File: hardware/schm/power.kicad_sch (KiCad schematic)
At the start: 14 parts, among them J1 VBUS input fly-leads, U2 AP63205WU-7

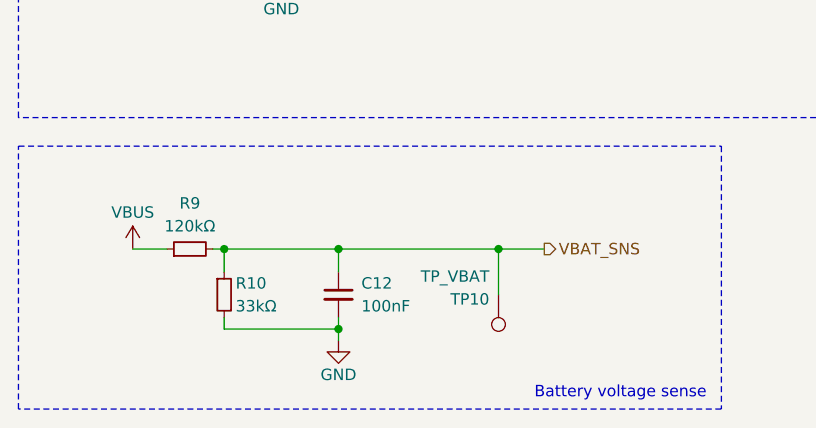
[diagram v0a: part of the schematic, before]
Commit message: feat: swap to the 74HC595 for cs expansion
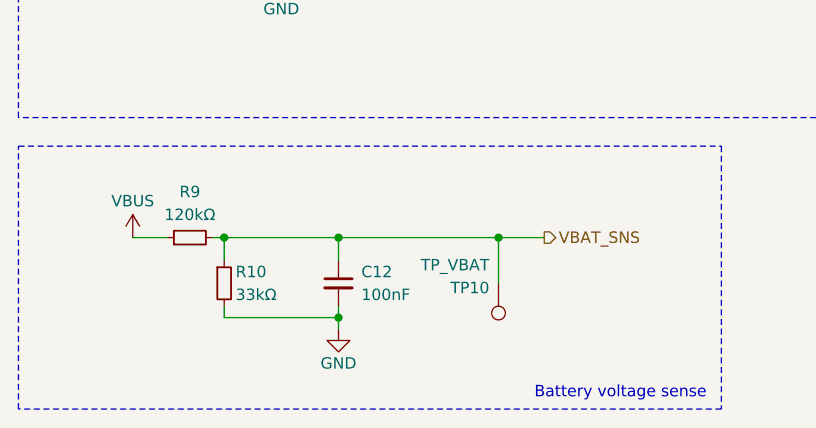
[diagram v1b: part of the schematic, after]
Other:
- moved on the sheet: C12, R10, R9, TP10
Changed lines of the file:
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@@
 	)
 	(junction
-		(at 68.58 74.93)
+		(at 68.58 73.66)
 		(diameter 0)
 		(color 0 0 0 0)
@@
 	)
 	(junction
-		(at 50.8 83.82)
+		(at 50.8 82.55)
 		(diameter 0)
 		(color 0 0 0 0)
 	)
 	(junction
-		(at 50.8 74.93)
+		(at 50.8 73.66)
 		(diameter 0)
 		(color 0 0 0 0)
 	)
 	(junction
-		(at 38.1 74.93)
+		(at 38.1 73.66)
 		(diameter 0)
 		(color 0 0 0 0)
@@
 	(wire
 		(pts
-			(xy 50.8 83.82) (xy 38.1 83.82)
+			(xy 50.8 82.55) (xy 38.1 82.55)
 		)
 		(stroke
@@
 	(wire
 		(pts
-			(xy 68.58 74.93) (xy 73.66 74.93)
+			(xy 68.58 73.66) (xy 73.66 73.66)
 		)
 		(stroke
@@
 	(wire
 		(pts
-			(xy 38.1 74.93) (xy 38.1 77.47)
+			(xy 38.1 73.66) (xy 38.1 76.2)
 		)
 		(stroke
@@
 	(wire
 		(pts
-			(xy 38.1 74.93) (xy 50.8 74.93)
+			(xy 38.1 73.66) (xy 50.8 73.66)
 		)
 		(stroke
@@
 	(wire
 		(pts
-			(xy 36.83 74.93) (xy 38.1 74.93)
+			(xy 36.83 73.66) (xy 38.1 73.66)
 		)
 		(stroke
@@
 	(wire
 		(pts
-			(xy 50.8 83.82) (xy 50.8 85.09)
-		)
-		(stroke
-			(width 0)
-			(type default)
-		)
-	)
-	(wire
-		(pts
-			(xy 68.58 74.93) (xy 68.58 80.01)
-		)
-		(stroke
-			(width 0)
-			(type default)
-		)
-	)
-	(wire
-		(pts
-			(xy 50.8 74.93) (xy 50.8 77.47)
+			(xy 50.8 82.55) (xy 50.8 83.82)
+		)
+		(stroke
+			(width 0)
+			(type default)
+		)
+	)
+	(wire
+		(pts
+			(xy 68.58 73.66) (xy 68.58 78.74)
+		)
+		(stroke
+			(width 0)
+			(type default)
+		)
+	)
+	(wire
+		(pts
+			(xy 50.8 73.66) (xy 50.8 76.2)
 		)
 		(stroke
@@
 	(wire
 		(pts
-			(xy 38.1 83.82) (xy 38.1 82.55)
+			(xy 38.1 82.55) (xy 38.1 81.28)
 		)
 		(stroke
@@
 	(wire
 		(pts
-			(xy 50.8 74.93) (xy 68.58 74.93)
+			(xy 50.8 73.66) (xy 68.58 73.66)
 		)
 		(stroke
@@
 	(wire
 		(pts
-			(xy 27.94 74.93) (xy 31.75 74.93)
+			(xy 27.94 73.66) (xy 31.75 73.66)
 		)
 		(stroke
@@
 	(wire
 		(pts
-			(xy 50.8 82.55) (xy 50.8 83.82)
+			(xy 50.8 81.28) (xy 50.8 82.55)
 		)
 		(stroke
@@
 	(hierarchical_label "VBAT_SNS"
 		(shape output)
-		(at 73.66 74.93 0)
+		(at 73.66 73.66 0)
 		(effects
 			(font
@@
 	(symbol
 		(lib_id "Device:R_Small")
-		(at 38.1 80.01 0)
+		(at 38.1 78.74 0)
 		(unit 1)
 		(body_style 1)
@@
 		(fields_autoplaced yes)
 		(property "Reference" "R10"
-			(at 39.37 78.74 0)
+			(at 39.37 77.47 0)
 			(show_name no)
 			(do_not_autoplace no)
@@
 		)
 		(property "Value" "33kΩ"
-			(at 39.37 81.28 0)
+			(at 39.37 80.01 0)
 			(show_name no)
 			(do_not_autoplace no)
@@
 		)
 		(property "Footprint" "Resistor_SMD:R_0402_1005Metric"
-			(at 38.1 80.01 0)
+			(at 38.1 78.74 0)
 			(hide yes)
 			(show_name no)
@@
 		)
 		(property "Datasheet" "~"
-			(at 38.1 80.01 0)
+			(at 38.1 78.74 0)
 			(hide yes)
 			(show_name no)
@@
 		)
 		(property "Description" ""
-			(at 38.1 80.01 0)
+			(at 38.1 78.74 0)
 			(show_name no)
 			(do_not_autoplace no)
@@
 		)
 		(property "LCSC Part" "NONE"
-			(at -312.42 -48.26 0)
+			(at -312.42 -49.53 0)
 			(hide yes)
 			(show_name no)
@@
 	(symbol
 		(lib_id "Device:R_Small")
-		(at 34.29 74.93 90)
+		(at 34.29 73.66 90)
 		(unit 1)
 		(body_style 1)
@@
 		(fields_autoplaced yes)
 		(property "Reference" "R9"
-			(at 34.29 69.85 90)
+			(at 34.29 68.58 90)
 			(show_name no)
 			(do_not_autoplace no)
@@
 		)
 		(property "Value" "120kΩ"
-			(at 34.29 72.39 90)
+			(at 34.29 71.12 90)
 			(show_name no)
 			(do_not_autoplace no)
@@
 		)
 		(property "Footprint" "Resistor_SMD:R_0402_1005Metric"
-			(at 34.29 74.93 0)
+			(at 34.29 73.66 0)
 			(hide yes)
 			(show_name no)
@@
 		)
 		(property "Datasheet" "~"
-			(at 34.29 74.93 0)
+			(at 34.29 73.66 0)
 			(hide yes)
 			(show_name no)
@@
 		)
 		(property "Description" ""
-			(at 34.29 74.93 0)
+			(at 34.29 73.66 0)
 			(show_name no)
 			(do_not_autoplace no)
@@
 		)
 		(property "LCSC Part" "NONE"
-			(at -83.82 425.45 0)
+			(at -83.82 424.18 0)
 			(hide yes)
 			(show_name no)
@@
 	(symbol
 		(lib_id "power:VBUS")
-		(at 27.94 74.93 0)
+		(at 27.94 73.66 0)
 		(unit 1)
 		(body_style 1)
@@
 		(dnp no)
 		(property "Reference" "#PWR075"
-			(at 27.94 71.12 0)
+			(at 27.94 69.85 0)
 			(hide yes)
 			(show_name no)
@@
 		)
 		(property "Value" "VBUS"
-			(at 27.94 70.866 0)
+			(at 27.94 69.596 0)
 			(show_name no)
 			(do_not_autoplace no)
@@
 		)
 		(property "Footprint" ""
-			(at 27.94 74.93 0)
+			(at 27.94 73.66 0)
 			(show_name no)
 			(do_not_autoplace no)
@@
 		)
 		(property "Datasheet" "~"
-			(at 27.94 74.93 0)
+			(at 27.94 73.66 0)
 			(hide yes)
 			(show_name no)
@@
 		)
 		(property "Description" ""
-			(at 27.94 74.93 0)
+			(at 27.94 73.66 0)
 			(show_name no)
 			(do_not_autoplace no)
@@
 	(symbol
 		(lib_id "power:GND")
-		(at 50.8 85.09 0)
+		(at 50.8 83.82 0)
 		(unit 1)
 		(body_style 1)
@@
 		(fields_autoplaced yes)
 		(property "Reference" "#PWR073"
+			(at 50.8 86.36 0)
+			(hide yes)
+			(show_name no)
+			(do_not_autoplace no)
+			(effects
+				(font
+					(size 1.27 1.27)
+				)
+			)
+		)
+		(property "Value" "GND"
 			(at 50.8 87.63 0)
-			(hide yes)
-			(show_name no)
-			(do_not_autoplace no)
-			(effects
-				(font
-					(size 1.27 1.27)
-				)
-			)
-		)
-		(property "Value" "GND"
-			(at 50.8 88.9 0)
 			(show_name no)
 			(do_not_autoplace no)
@@
 		)
 		(property "Footprint" ""
-			(at 50.8 85.09 0)
+			(at 50.8 83.82 0)
 			(show_name no)
 			(do_not_autoplace no)
@@
 		)
 		(property "Datasheet" "~"
-			(at 50.8 85.09 0)
+			(at 50.8 83.82 0)
 			(hide yes)
 			(show_name no)
@@
 		)
 		(property "Description" ""
-			(at 50.8 85.09 0)
+			(at 50.8 83.82 0)
 			(show_name no)
 			(do_not_autoplace no)
@@
 	(symbol
 		(lib_id "Connector:TestPoint")
-		(at 68.58 80.01 180)
+		(at 68.58 78.74 180)
 		(unit 1)
 		(body_style 1)
@@
 		(dnp no)
 		(property "Reference" "TP10"
-			(at 67.564 80.518 0)
+			(at 67.564 79.248 0)
 			(show_name no)
 			(do_not_autoplace no)
@@
 		)
 		(property "Value" "TP_VBAT"
-			(at 67.564 77.978 0)
+			(at 67.564 76.708 0)
 			(show_name no)
 			(do_not_autoplace no)
@@
 		)
 		(property "Footprint" "TestPoint:TestPoint_Pad_D1.0mm"
-			(at 68.58 80.01 0)
+			(at 68.58 78.74 0)
 			(hide yes)
 			(show_name no)
@@
 		)
 		(property "Datasheet" "~"
-			(at 68.58 80.01 0)
+			(at 68.58 78.74 0)
 			(hide yes)
 			(show_name no)
@@
 		)
 		(property "Description" ""
-			(at 68.58 80.01 0)
+			(at 68.58 78.74 0)
 			(show_name no)
 			(do_not_autoplace no)
@@
 		)
 		(property "LCSC Part" "NONE"
-			(at 412.75 203.2 0)
+			(at 412.75 201.93 0)
 			(hide yes)
 			(show_name no)
@@
 	(symbol
 		(lib_id "Device:C_Small")
-		(at 50.8 80.01 0)
+		(at 50.8 78.74 0)
 		(unit 1)
 		(body_style 1)
@@
 		(fields_autoplaced yes)
 		(property "Reference" "C12"
-			(at 53.34 78.74 0)
+			(at 53.34 77.47 0)
 			(show_name no)
 			(do_not_autoplace no)
@@
 		)
 		(property "Value" "100nF"
-			(at 53.34 81.28 0)
+			(at 53.34 80.01 0)
 			(show_name no)
 			(do_not_autoplace no)
@@
 		)
 		(property "Footprint" "Capacitor_SMD:C_0402_1005Metric"
-			(at 50.8 80.01 0)
+			(at 50.8 78.74 0)
 			(hide yes)
 			(show_name no)
@@
 		)
 		(property "Datasheet" "~"
-			(at 50.8 80.01 0)
+			(at 50.8 78.74 0)
 			(hide yes)
 			(show_name no)
@@
 		)
 		(property "Description" ""
-			(at 50.8 80.01 0)
+			(at 50.8 78.74 0)
 			(show_name no)
 			(do_not_autoplace no)
@@
 		)
 		(property "LCSC Part" "NONE"
-			(at -307.34 -45.72 0)
-			(hide yes)
-			(show_name no)
+			(at -307.34 -46.99 0)
+			(hide yes)
+			(show_name no)

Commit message: feat: first bit of routing and double leds + fixes
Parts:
- added C13: 10uF, Capacitor_SMD:C_0603_1608Metric, symbol Device:C_Small
- J1: footprint Connector_Wire:SolderWire-0.5sqmm_1x02_P4.6mm_D0.9mm_OD2.1mm_Relief -> Connector_Wire:SolderWire-0.25sqmm_1x02_P4.2mm_D0.65mm_OD1.7mm
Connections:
- net 3V3: now also C13.1
- net GND: now also C13.2
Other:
- moved on the sheet: C6

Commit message: feat: add bom placement
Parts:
- C1, C4, C5: LCSC Part NONE -> C602037
- C12, C2, C3: LCSC Part NONE -> C169834
- C13, C6: LCSC Part NONE -> C913532
- J1, TP10: now left out of the parts list
- R10: value 33kΩ -> 33.2kΩ; LCSC Part NONE -> C3008937
- R9: LCSC Part NONE -> C409883
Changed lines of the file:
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@@
 			)
 		)
-		(property "LCSC Part" "NONE"
+		(property "LCSC Part" "C169834"
 			(at 152.4 -59.69 0)
 			(hide yes)
@@
 			)
 		)
-		(property "LCSC Part" "NONE"
+		(property "LCSC Part" "C169834"
 			(at 17.78 1.27 0)
 			(hide yes)
@@
 			)
 		)
-		(property "Value" "33kΩ"
+		(property "Value" "33.2kΩ"
 			(at 39.37 80.01 0)
 			(show_name no)
@@
 			)
 		)
-		(property "LCSC Part" "NONE"
+		(property "LCSC Part" "C3008937"
 			(at -312.42 -49.53 0)
 			(hide yes)
@@
 			)
 		)
-		(property "LCSC Part" "NONE"
+		(property "LCSC Part" "C602037"
 			(at 26.67 3.81 0)
 			(hide yes)
@@
 			)
 		)
-		(property "LCSC Part" "NONE"
+		(property "LCSC Part" "C409883"
 			(at -83.82 424.18 0)
 			(hide yes)
@@
 			)
 		)
-		(property "LCSC Part" "NONE"
+		(property "LCSC Part" "C602037"
 			(at 26.67 3.81 0)
 			(hide yes)
@@
 			)
 		)
-		(property "LCSC Part" "NONE"
+		(property "LCSC Part" "C913532"
 			(at 21.59 2.54 0)
 			(hide yes)
@@
 			)
 		)
-		(property "LCSC Part" "NONE"
+		(property "LCSC Part" "C913532"
 			(at 31.75 2.54 0)
 			(hide yes)
@@
 			)
 		)
-		(property "LCSC Part" "NONE"
+		(property "LCSC Part" "C602037"
 			(at 17.78 1.27 0)
 			(hide yes)
@@
 		(body_style 1)
 		(exclude_from_sim no)
-		(in_bom yes)
-		(on_board yes)
-		(in_pos_files yes)
+		(in_bom no)
+		(on_board yes)
+		(in_pos_files no)
 		(dnp no)
 		(property "Reference" "TP10"
@@
 			)
 		)
-		(property "LCSC Part" "NONE"
+		(property "LCSC Part" "C169834"
 			(at -307.34 -46.99 0)
 			(hide yes)
@@
 		(body_style 1)
 		(exclude_from_sim no)
-		(in_bom yes)
-		(on_board yes)
-		(in_pos_files yes)
+		(in_bom no)
+		(on_board yes)
+		(in_pos_files no)
 		(dnp no)
 		(fields_autoplaced yes)

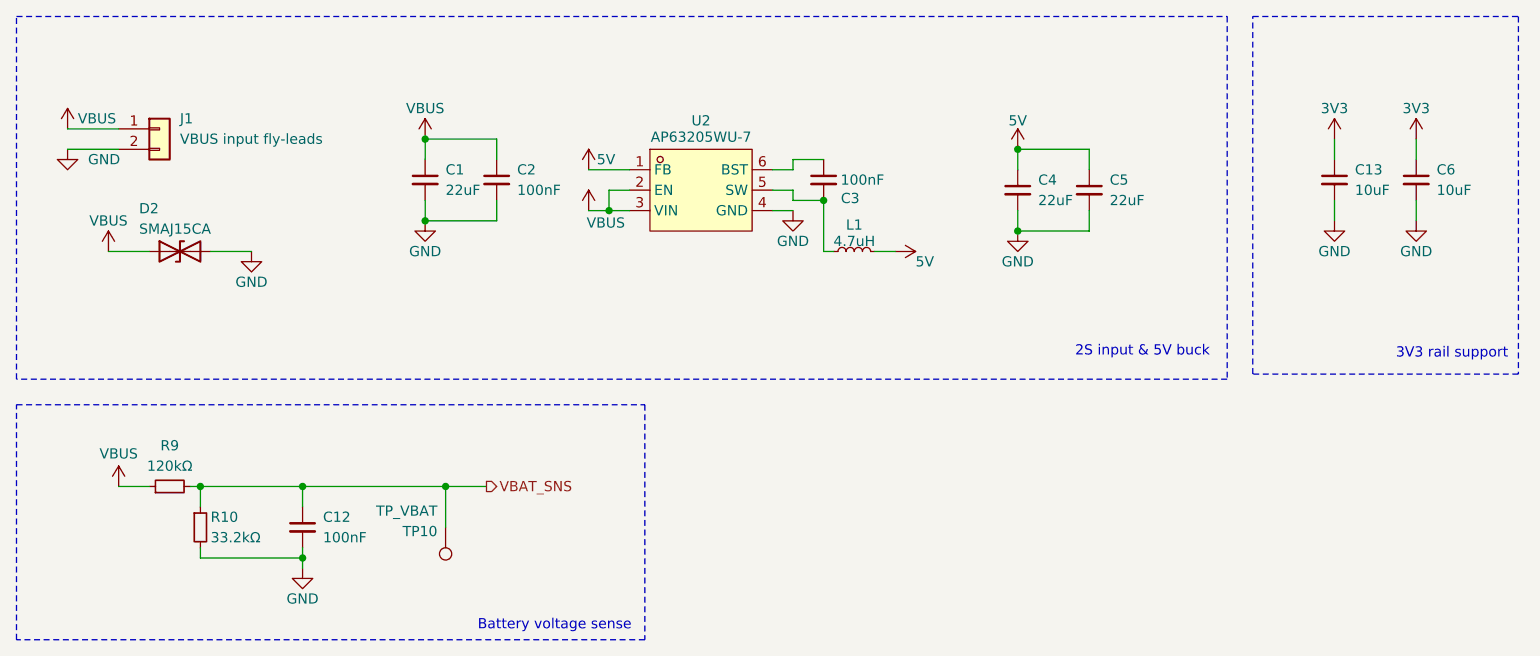
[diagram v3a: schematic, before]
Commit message: feat: review from tyler + align circuit.py
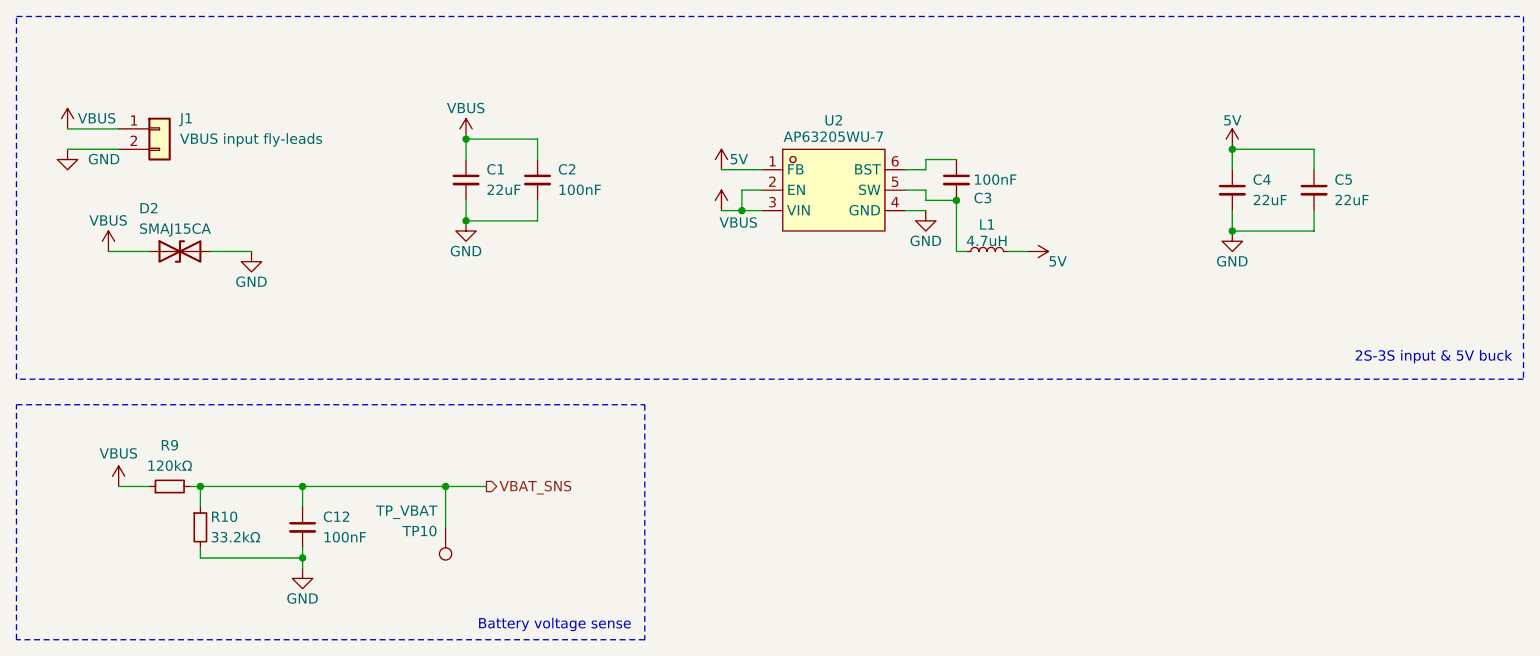
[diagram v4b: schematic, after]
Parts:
- removed C13, C6: 10uF, Capacitor_SMD:C_0603_1608Metric, symbol Device:C_Small
- D2: LCSC Part C110042 -> C110044
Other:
- note added: "2S-3S input & 5V buck"
- note removed: "2S input & 5V buck"
- note removed: "3V3 rail support"
- moved on the sheet: C1, C2, C3, C4, C5, L1, U2

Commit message: feat: add jumper for shutoff voltage
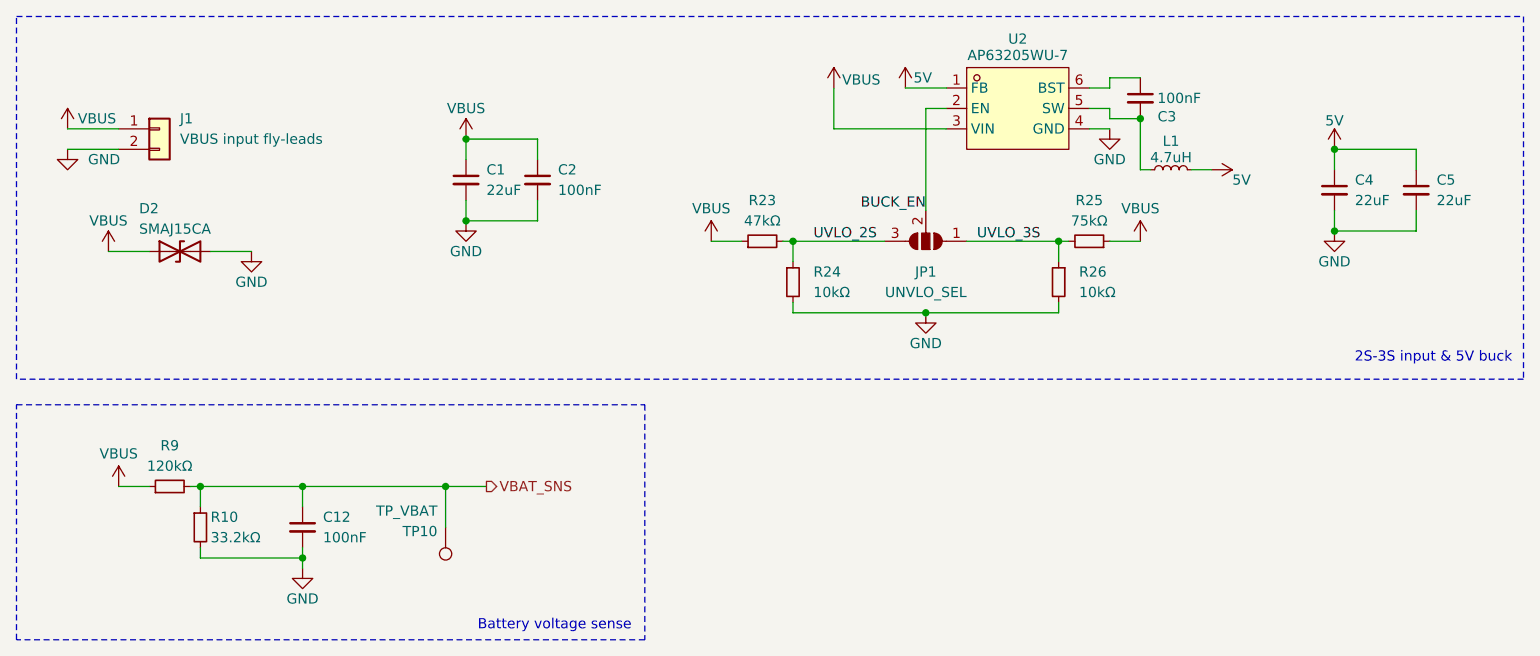
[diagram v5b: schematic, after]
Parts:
- added JP1: UNVLO_SEL, Jumper:SolderJumper-3_P1.3mm_Open_Pad1.0x1.5mm, symbol Jumper:SolderJumper_3_Open
- added R23: 47kΩ, Resistor_SMD:R_0402_1005Metric, symbol Device:R_Small
- added R24, R26: 10kΩ, Resistor_SMD:R_0402_1005Metric, symbol Device:R_Small
- added R25: 75kΩ, Resistor_SMD:R_0402_1005Metric, symbol Device:R_Small
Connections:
- net GND: now also R24.2, R26.2
- net VBUS: now also R23.1, R25.1; no longer U2.2 (EN)
- new net BUCK_EN: JP1.2 (C), U2.2 (EN)
- new net UVLO_2S: JP1.3 (B), R23.2, R24.1
- new net UVLO_3S: JP1.1 (A), R25.2, R26.1
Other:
- moved on the sheet: C3, C4, C5, L1, U2
